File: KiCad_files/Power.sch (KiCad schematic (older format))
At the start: 82 parts, among them J2 PCIe_6_Pin_Power, Q1 Q_NMOS_DGS, Q2 Q_PMOS_DGS, U2 PI3420, U3 PI3421, U4 PI3420

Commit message: Cleanup for demo/presentation
Merged Config and Debug sheets.
Added GPIO for remaining pins.
Annotations.
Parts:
- gave numbers to parts that had none: 6
- renumbered C13 to C15, C14 to C16, C15 to C17, C16 to C18, C17 to C19, C18 to C20, C19 to C21, C20 to C22, C21 to C23, C22 to C24, C23 to C25, C24 to C26, C25 to C27, C26 to C28, C27 to C29, C28 to C30, C29 to C31, C30 to C32, C31 to C33, C32 to C34, C33 to C35, C34 to C36, C35 to C37, C36 to C38, C37 to C39, C38 to C40, C39 to C41, C40 to C42, C41 to C43, C42 to C44, C43 to C45, C44 to C46, C45 to C47, C46 to C48, C47 to C49, C48 to C50, C49 to C51, C50 to C52, C51 to C53, C52 to C54, C53 to C55, C54 to C56, C55 to C57, C56 to C58, C57 to C59, C58 to C60, C59 to C61, C60 to C62, C61 to C63, C62 to C64, C63 to C65, C64 to C66, C65 to C67, C66 to C68, R3 to R5, R4 to R6, U2 to U3, U3 to U4, U4 to U5

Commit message: Cleanup + Update to KiCad 5.0 + DDR2
Updated to KiCad 5, which re-organized libraries, so corrected them to not need RASAC-rescue.lib.
Also cleaned up some stuff.
DDR4 has been removed and in place will be DDR2.
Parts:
- C11: symbol C -> Device:C
- C12: symbol CP1 -> Device:CP1
- C13, C14, C15, C16, C17, C18, C19, C20, C21, C22, C23, C24, C25, C26, C27, C28, C29, C30, C31, C32, C33, C34, C35, C36, C37, C38, C39, C40, C41, C42, C43, C44, C45, C46, C47, C48, C49, C50, C51, C52, C53, C54, C55, C56, C57, C58, C59, C60, C61, C62, C63, C64, C65, C66, C67, C68: symbol C_Small -> Device:C_Small
- D1: symbol D_Zener -> Device:D_Zener
- D2: symbol LED -> Device:LED
- J2: symbol PCIe_6_Pin_Power -> custom:PCIe_6_Pin_Power
- L1, L2, L3: symbol L -> Device:L
- Q1: symbol Q_NMOS_DGS -> Device:Q_NMOS_DGS
- Q2: symbol Q_PMOS_DGS -> Device:Q_PMOS_DGS
- R2, R3, R4, R5, R6: symbol R -> Device:R
- U1: symbol XC7A35T_CSG325 -> custom:XC7A35T_CSG325
- U2: symbol MAX15027 -> custom:MAX15027
- U3, U5: symbol PI3420 -> custom:PI3420
- U4: symbol PI3421 -> custom:PI3421
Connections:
- wire segments 231 -> 403
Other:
- note added: "SYSCLK needs 2.5V"
- note removed: "RAM needs 2.5V\nSYSCLK needs 2.5V"

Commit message: More fixes
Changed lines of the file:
@@
 $EndComp
 $Comp
-L power:GND- #PWR066
+L power:GND #PWR066
 U 1 1 5C05D184
 P 8500 1300

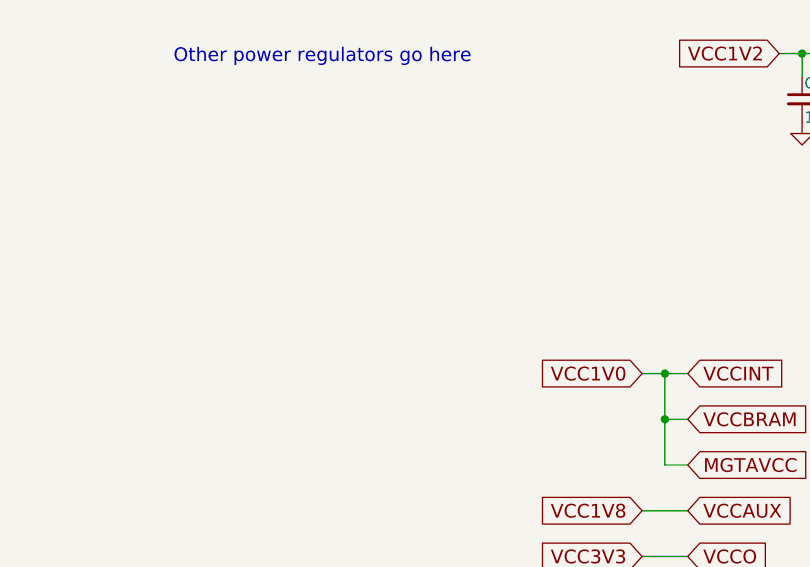
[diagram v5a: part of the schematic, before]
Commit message: HDMI_VGA is good. Need 5V for HDMI
TODO: DDR2, connections, power
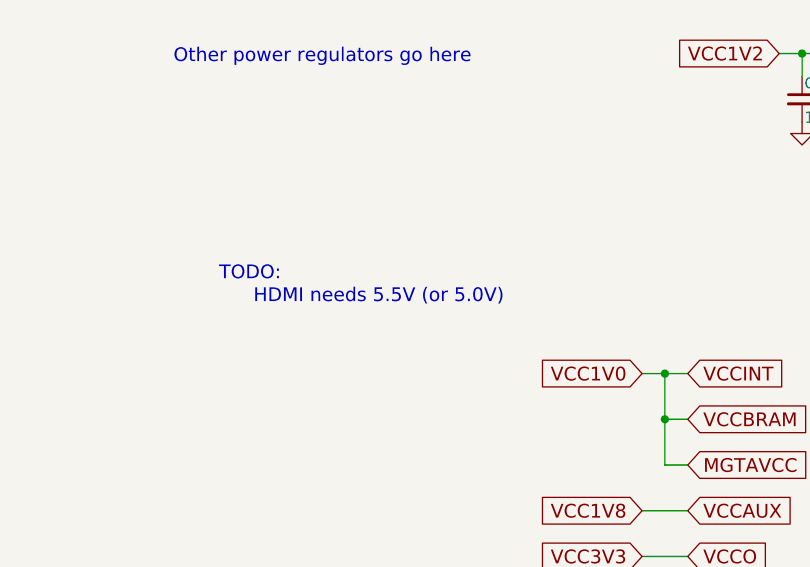
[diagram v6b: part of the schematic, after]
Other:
- note added: "HDMI needs 5.5V (or 5.0V)"
- note added: "TODO:"
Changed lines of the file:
@@
 $Descr A4 11693 8268
 encoding utf-8
-Sheet 3 10
+Sheet 3 9
 Title "Reconfigurable Application-Specific Accelerator Card"
 Date "2018-11-27"
@@
 Wire Wire Line
 	5500 3450 5800 3450
+Text Notes 4350 5900 0    60   ~ 0
+HDMI needs 5.5V (or 5.0V)
+Text Notes 4200 5800 0    60   ~ 0
+TODO:
 $EndSCHEMATC

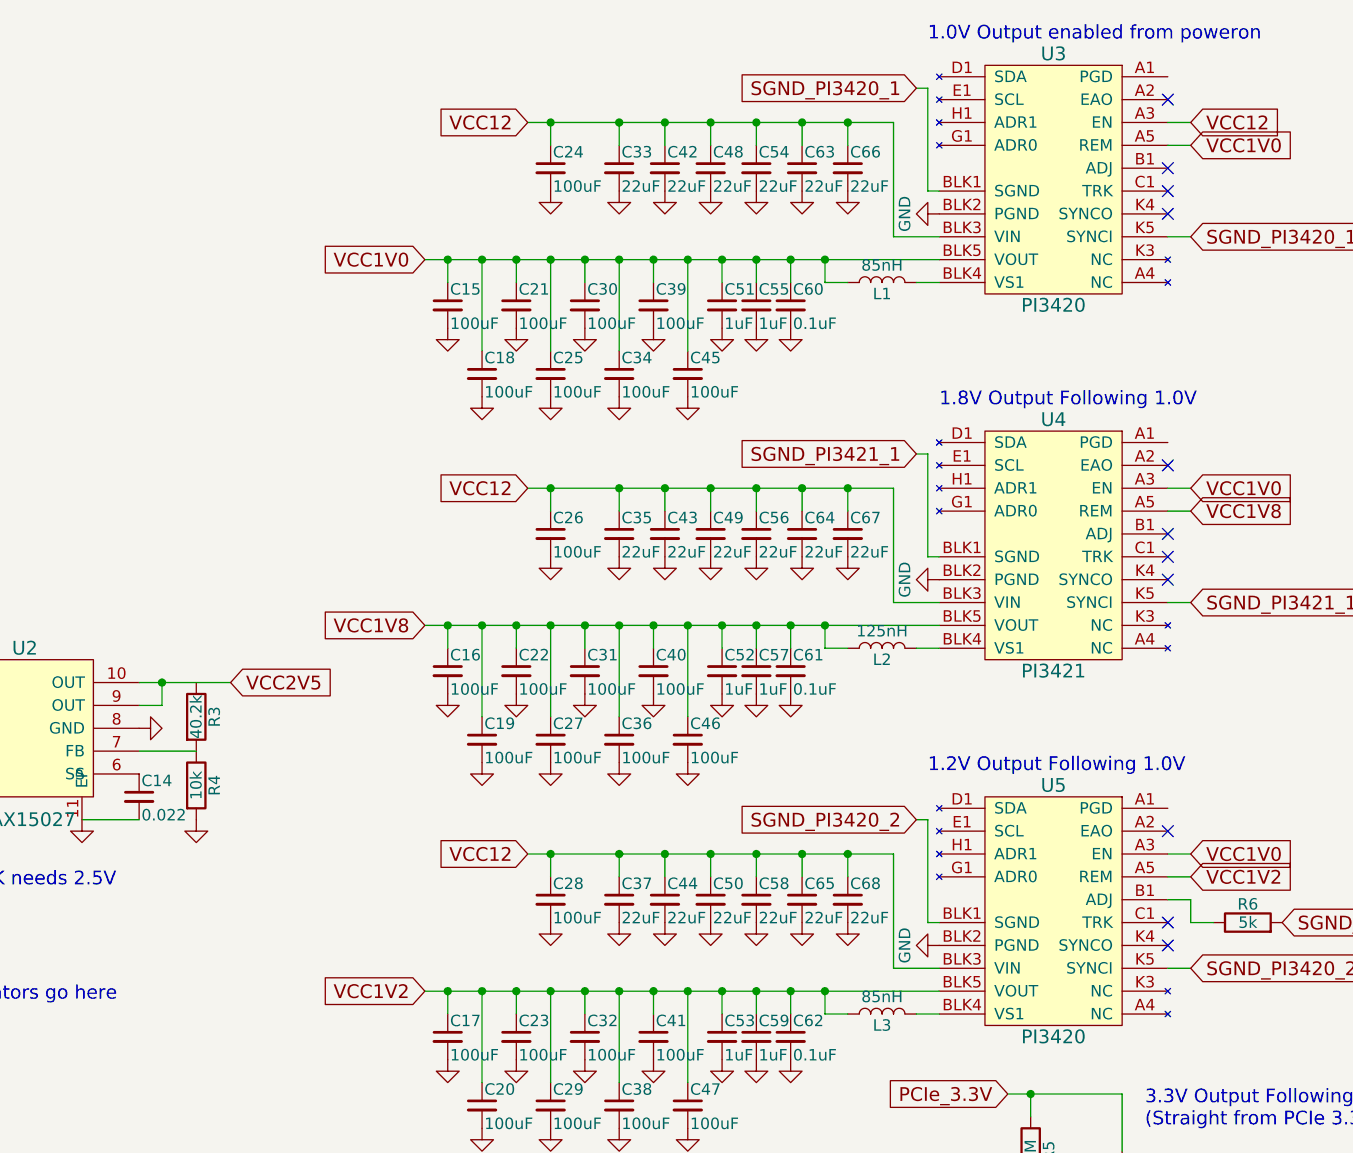
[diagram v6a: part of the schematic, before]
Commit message: Cleanup for DRC and HDMI. HDMI and DDR2 looks good
DRC returns 5 errors with POWEROUTPUT-POWEROUTPUT set as good.
3 of them come from 3V3 since it's being driven from a MOSFET.
1 of them from VCC5V0 not yet supplied.
1 of them from USB_VBUS not set as output.
TODO:
5V supply for HDMI
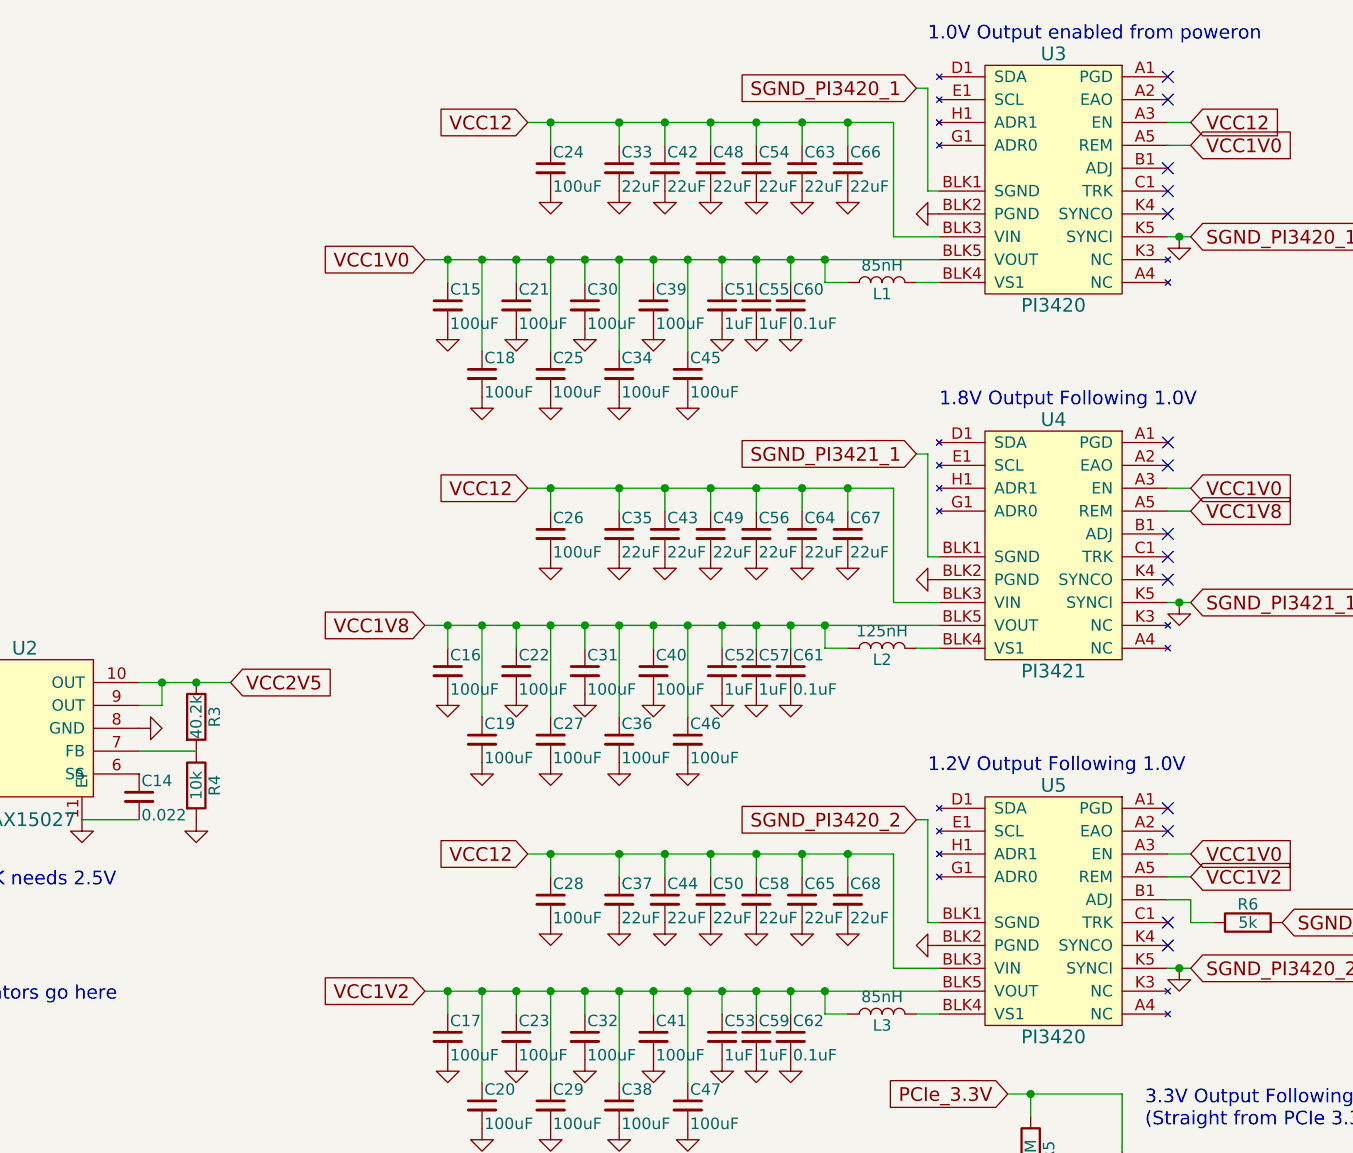
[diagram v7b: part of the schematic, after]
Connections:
- net SGND_PI3420_1 is gone; now on net GND: U3.BLK1 (SGND), U3.K5 (SYNCI)
- net SGND_PI3420_2 is gone; now on net GND: R6.2, U5.BLK1 (SGND), U5.K5 (SYNCI)
- net SGND_PI3421_1 is gone; now on net GND: U4.BLK1 (SGND), U4.K5 (SYNCI)
- net VCC2V5: now also R3.1
- no-connect marks 12 -> 15
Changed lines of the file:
@@
 U 1 1 5BFF1B6E
 P 9400 1250
+AR Path="/5BFF1B6E" Ref="U3"  Part="1"
+AR Path="/5BFDDAF0/5BFF1B6E" Ref="U3"  Part="1"
 F 0 "U3" H 9400 1800 60  0000 C CNN
 F 1 "PI3420" H 9400 700 60  0000 C CNN
@@
 P 8900 1400
 F 0 "#PWR069" H 8900 1150 50  0001 C CNN
-F 1 "GND" H 8900 1250 50  0000 C CNN
+F 1 "GND" H 8900 1250 50  0001 C CNN
 F 2 "" H 8900 1400 50  0001 C CNN
 F 3 "" H 8900 1400 50  0001 C CNN
@@
 P 8900 3000
 F 0 "#PWR070" H 8900 2750 50  0001 C CNN
-F 1 "GND" H 8900 2850 50  0000 C CNN
+F 1 "GND" H 8900 2850 50  0001 C CNN
 F 2 "" H 8900 3000 50  0001 C CNN
 F 3 "" H 8900 3000 50  0001 C CNN
@@
 U 1 1 5C060E07
 P 9400 2850
+AR Path="/5C060E07" Ref="U4"  Part="1"
+AR Path="/5BFDDAF0/5C060E07" Ref="U4"  Part="1"
 F 0 "U4" H 9400 3400 60  0000 C CNN
 F 1 "PI3421" H 9400 2300 60  0000 C CNN
@@
 U 1 1 5C06270E
 P 9400 4450
+AR Path="/5C06270E" Ref="U5"  Part="1"
+AR Path="/5BFDDAF0/5C06270E" Ref="U5"  Part="1"
 F 0 "U5" H 9400 5000 60  0000 C CNN
 F 1 "PI3420" H 9400 3900 60  0000 C CNN
@@
 P 8900 4600
 F 0 "#PWR071" H 8900 4350 50  0001 C CNN
-F 1 "GND" H 8900 4450 50  0000 C CNN
+F 1 "GND" H 8900 4450 50  0001 C CNN
 F 2 "" H 8900 4600 50  0001 C CNN
 F 3 "" H 8900 4600 50  0001 C CNN
@@
 	10000 1100 9900 1100
 Wire Wire Line
-	10000 1500 9900 1500
+	10000 1500 9950 1500
 Wire Wire Line
 	6650 1600 6750 1600
@@
 	10000 2700 9900 2700
 Wire Wire Line
-	10000 3100 9900 3100
+	10000 3100 9950 3100
 Wire Wire Line
 	6650 3200 6750 3200
@@
 	10000 4300 9900 4300
 Wire Wire Line
-	10000 4700 9900 4700
+	10000 4700 9950 4700
 Wire Wire Line
 	6650 4800 6750 4800
@@
 Wire Wire Line
 	9700 5900 9700 5950
-Wire Wire Line
-	9700 5950 9900 5950
 Text GLabel 9000 5950 0    60   Input ~ 0
 VCC1V8
@@
 Wire Wire Line
 	5500 3550 5400 3550
-Connection ~ 5500 3450
 $Comp
 L power:GND #PWR013
@@
 U 1 1 5C13DD12
 P 4900 3650
+AR Path="/5C13DD12" Ref="U2"  Part="1"
+AR Path="/5BFDDAF0/5C13DD12" Ref="U2"  Part="1"
 F 0 "U2" H 4900 4000 60  0000 C CNN
 F 1 "MAX15027" H 4900 3250 60  0000 C CNN
@@
 U 8 1 5C174146
 P 1400 7200
+AR Path="/5C174146" Ref="U1"  Part="8"
+AR Path="/5BFDDAF0/5C174146" Ref="U1"  Part="8"
 F 0 "U1" H 1400 6900 60  0000 C CNN
 F 1 "XC7A35T_CSG325" H 1400 7000 60  0000 C CNN
@@
 U 9 1 5C174229
 P 2600 7200
+AR Path="/5C174229" Ref="U1"  Part="9"
+AR Path="/5BFDDAF0/5C174229" Ref="U1"  Part="9"
 F 0 "U1" H 2600 6900 60  0000 C CNN
 F 1 "XC7A35T_CSG325" H 2600 7000 60  0000 C CNN
@@
 U 10 1 5C1742F8
 P 1200 3100
+AR Path="/5C1742F8" Ref="U1"  Part="10"
+AR Path="/5BFDDAF0/5C1742F8" Ref="U1"  Part="10"
 F 0 "U1" H 1200 2800 60  0000 C CNN
 F 1 "XC7A35T_CSG325" H 1200 2900 60  0000 C CNN
@@
 U 11 1 5C1743D9
 P 1150 3900
+AR Path="/5C1743D9" Ref="U1"  Part="11"
+AR Path="/5BFDDAF0/5C1743D9" Ref="U1"  Part="11"
 F 0 "U1" H 1150 3600 60  0000 C CNN
 F 1 "XC7A35T_CSG325" H 1150 3700 60  0000 C CNN
@@
 U 12 1 5C1744A4
 P 1150 4800
+AR Path="/5C1744A4" Ref="U1"  Part="12"
+AR Path="/5BFDDAF0/5C1744A4" Ref="U1"  Part="12"
 F 0 "U1" H 1150 4500 60  0000 C CNN
 F 1 "XC7A35T_CSG325" H 1150 4600 60  0000 C CNN
@@
 U 6 1 5C1747A8
 P 1150 2400
+AR Path="/5C1747A8" Ref="U1"  Part="6"
+AR Path="/5BFDDAF0/5C1747A8" Ref="U1"  Part="6"
 F 0 "U1" H 1150 2100 60  0000 C CNN
 F 1 "XC7A35T_CSG325" H 1150 2200 60  0000 C CNN
@@
 U 7 1 5C174893
 P 2550 4800
+AR Path="/5C174893" Ref="U1"  Part="7"
+AR Path="/5BFDDAF0/5C174893" Ref="U1"  Part="7"
 F 0 "U1" H 2550 4500 60  0000 C CNN
 F 1 "XC7A35T_CSG325" H 2550 4600 60  0000 C CNN
@@
 Wire Wire Line
 	4300 3650 4300 3850
-Wire Wire Line
-	5500 3450 5800 3450
 Text Notes 4350 5900 0    60   ~ 0
 HDMI needs 5.5V (or 5.0V)
 Text Notes 4200 5800 0    60   ~ 0
 TODO:
+NoConn ~ 9900 2400
+NoConn ~ 9900 4000
+NoConn ~ 9900 800
+Wire Wire Line
+	5500 3450 5650 3450
+Connection ~ 5500 3450
+Wire Wire Line
+	5800 3450 5650 3450
+Connection ~ 5650 3450
+$Comp
+L power:GND #PWR0122
+U 1 1 5C8C264C
+P 9950 1500
+F 0 "#PWR0122" H 9950 1250 50  0001 C CNN
+F 1 "GND" H 9950 1350 50  0001 C CNN
+F 2 "" H 9950 1500 50  0001 C CNN
+F 3 "" H 9950 1500 50  0001 C CNN
+	1    9950 1500
+	1    0    0    -1
+$EndComp
+Connection ~ 9950 1500
+Wire Wire Line
+	9950 1500 9900 1500
+$Comp
+L power:GND #PWR0123
+U 1 1 5C8C27F3
+P 9950 3100
+F 0 "#PWR0123" H 9950 2850 50  0001 C CNN
+F 1 "GND" H 9950 2950 50  0001 C CNN
+F 2 "" H 9950 3100 50  0001 C CNN
+F 3 "" H 9950 3100 50  0001 C CNN
+	1    9950 3100
+	1    0    0    -1
+$EndComp
+Connection ~ 9950 3100
+Wire Wire Line
+	9950 3100 9900 3100
+$Comp
+L power:GND #PWR0130
+U 1 1 5C8C2AA0
+P 9950 4700
+F 0 "#PWR0130" H 9950 4450 50  0001 C CNN
+F 1 "GND" H 9950 4550 50  0001 C CNN
+F 2 "" H 9950 4700 50  0001 C CNN
+F 3 "" H 9950 4700 50  0001 C CNN
+	1    9950 4700
+	1    0    0    -1
+$EndComp
+Connection ~ 9950 4700
+Wire Wire Line
+	9950 4700 9900 4700
+Wire Wire Line
+	9700 5950 9900 5950
 $EndSCHEMATC
